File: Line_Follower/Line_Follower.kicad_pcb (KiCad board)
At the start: 2 copper layers, 109 x 110.5 mm, 20 parts, among them J1 Battery terminal, J10 Motor_B, J11 8-Channel IR Array, J9 Motor_A, SW1 Slide Switch, SW3 Mode, SW6 Calibration, U1 ESP32-DEVKITC, U2 LM2596 Buck Converter, U3 TB6612FNG_MD

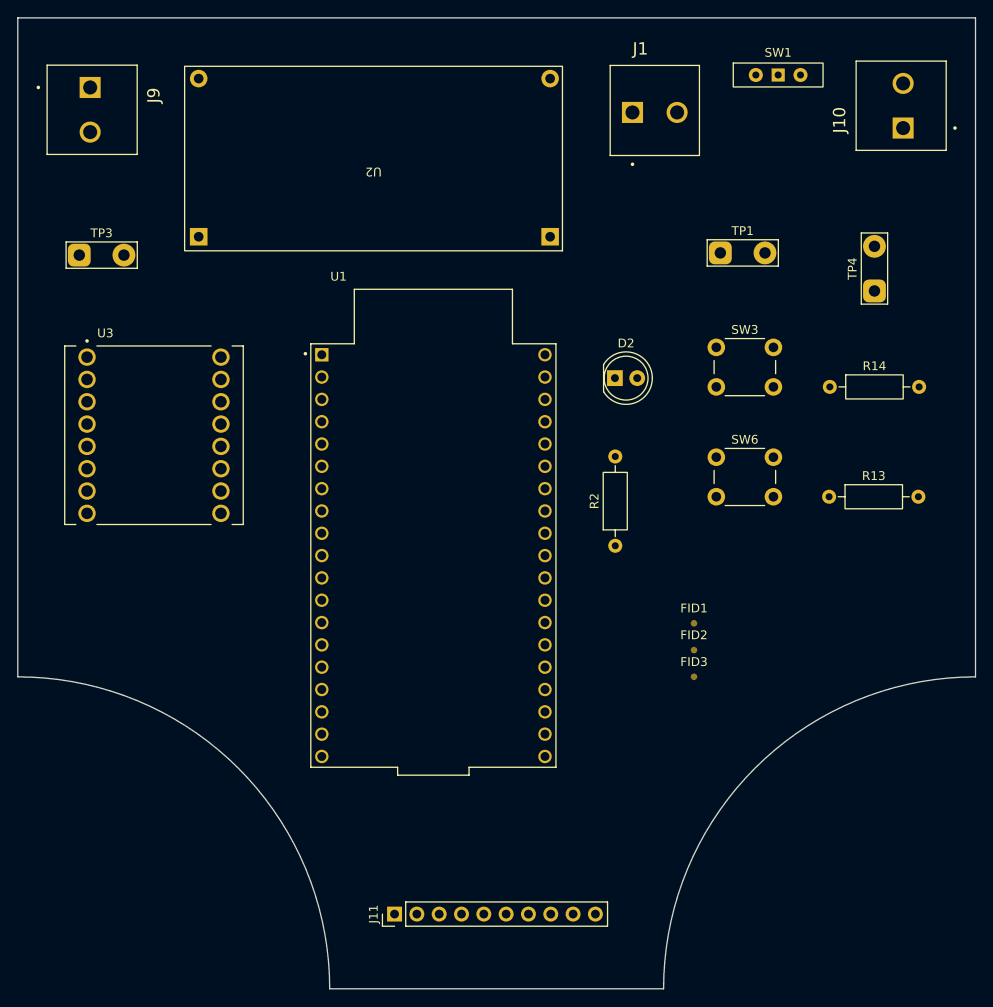
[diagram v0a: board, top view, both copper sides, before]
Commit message: PCB edge cuts designed
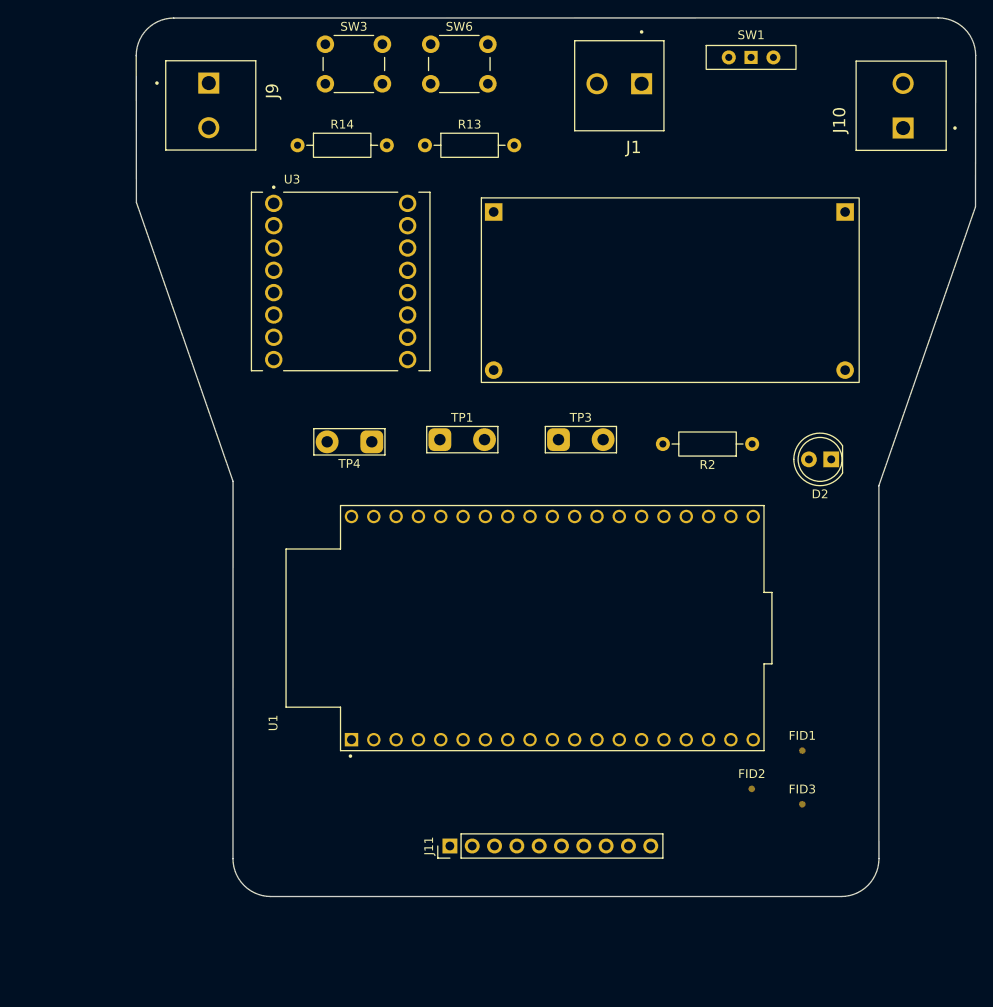
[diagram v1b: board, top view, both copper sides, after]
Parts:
- moved R14 66.5 mm to (116.8, 44.5)
- moved R13 61.0 mm to (131.3, 44.5)
- moved TP4 59.7 mm to (125.3, 78.2), turned to 180 degrees
- moved TP3 58.4 mm to (146.5, 78.0)
- moved SW6 57.1 mm to (132.0, 33.0)
- moved SW3 56.3 mm to (120.0, 33.0)
- moved TP1 38.3 mm to (133.0, 78.0)
- moved U2 37.1 mm to (137.8, 71.5), turned to 0 degrees
- moved U3 27.5 mm to (121.8, 60.0)
- moved D2 26.3 mm to (177.6, 80.2), turned to 180 degrees
- moved R2 19.4 mm to (168.6, 78.5), turned to 180 degrees
- moved FID1 19.0 mm to (174.3, 113.4)
- moved FID3 19.0 mm to (174.3, 119.5)
- moved FID2 17.1 mm to (168.5, 117.8)
- moved U1 15.9 mm to (145.8, 99.5), turned to 90 degrees
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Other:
- board size 109 x 110.5 mm -> 95.5 x 100 mm

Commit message: PCB updated
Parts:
- TP1: footprint TestPoint:TestPoint_2Pads_Pitch5.08mm_Drill1.3mm -> TestPoint:TestPoint_Pad_2.0x2.0mm
- TP2: renamed from TP4; footprint TestPoint:TestPoint_2Pads_Pitch5.08mm_Drill1.3mm -> TestPoint:TestPoint_Pad_2.0x2.0mm
- moved SW6 9.78 mm to (141.8, 33.8)
- moved R14 9.30 mm to (126.1, 45.5)
- moved SW3 9.30 mm to (129.2, 34.0)
- moved R13 9.06 mm to (140.3, 45.5)
- moved J1 4.75 mm to (160.8, 37.5)
- moved SW1 3.37 mm to (171.8, 34.0)
- moved U1 1.98 mm to (147.8, 99.7)
- moved U3 1.50 mm to (121.8, 61.5)
- moved U2 1.12 mm to (137.3, 72.5)
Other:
- board text added: "+"
- board text added: "+LED-"
- board text added: "-"
- board text added: "10K"
- board text added: "220"
- board text added: "3.3V"
- board text added: "Calib"
- board text added: "GND"
- board text added: "IR Array"
- board text added: "IR1"
- board text added: "IR2"
- board text added: "IR3"
- board text added: "IR4"
- board text added: "IR5"
- board text added: "IR6"
- board text added: "IR7"
- board text added: "IR8"
- board text added: "MA"
- board text added: "MB"
- board text added: "Mode"
- board text added: "Power"
- board text added: "V_BAT"

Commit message: PCB edited
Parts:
- removed FID1, FID2, FID3: Fiducial, Fiducial:Fiducial_0.75mm_Mask1.5mm
- removed TP3: TP_3V3, TestPoint:TestPoint_2Pads_Pitch5.08mm_Drill1.3mm
- moved TP1 44.8 mm to (119.8, 35.2), turned to 180 degrees
- moved TP2 43.3 mm to (125.2, 35.0), turned to 0 degrees
- moved D2 25.1 mm to (152.5, 78.8)
- moved SW3 2.71 mm to (132.0, 34.0)
- moved U2 1.75 mm to (135.5, 72.5)
- moved U1 1.74 mm to (146.6, 98.5)
- moved SW6 1.52 mm to (143.2, 34.0)
- moved U3 0.38 mm to (121.4, 61.5)
- moved SW1 0.37 mm to (172.1, 34.2)
- moved J1 0.37 mm to (161.0, 37.7)
- moved R13 0.37 mm to (140.6, 45.7)
- moved R14 0.37 mm to (126.4, 45.7)

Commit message: PCB updated
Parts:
- added H1: MountingHole, MountingHole:MountingHole_3.2mm_M3, F.Cu at (105.0, 54.5)
- added H2: MountingHole, MountingHole:MountingHole_3.2mm_M3, F.Cu at (187.5, 54.5)
- added H3: MountingHole, MountingHole:MountingHole_3.2mm_M3, F.Cu at (116.2, 115.8)
- added H4: MountingHole, MountingHole:MountingHole_3.2mm_M3, F.Cu at (176.2, 115.8)
- moved D2 41.7 mm to (176.2, 44.5)
- moved R2 29.2 mm to (167.8, 49.3), turned to 90 degrees
- moved J11 9.52 mm to (134.8, 114.8)
- moved U1 5.31 mm to (148.4, 93.5)
- moved U2 2.85 mm to (137.3, 74.7)
- moved U3 2.41 mm to (122.6, 63.6)
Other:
- board size 95.5 x 100 mm -> 95.5 x 93.5 mm
- board text removed: "IR Array"

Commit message: 3D models added
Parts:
- moved SW3 2.72 mm to (129.2, 34.3)
- moved SW6 2.72 mm to (140.5, 34.2)
- moved TP1 2.72 mm to (117.0, 35.5)
- moved TP2 2.72 mm to (122.5, 35.3)
- moved J1 2.72 mm to (158.3, 38.0)
- moved SW1 0.87 mm to (171.2, 34.2)
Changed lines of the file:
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@@
 	(footprint "Button_Switch_THT:SW_Slide-03_Wuerth-WS-SLTV_10x2.5x6.4_P2.54mm"
 		(layer "F.Cu")
-		(at 172.08 34.2375)
+		(at 171.21 34.2375)
 		(descr "Wuerth, WS-SLTV, 450301014042, https://www.we-online.com/components/products/datasheet/450301014042.pdf")
 		(tags "switch single-pole opposite-side-connection double-throw SPDT würth wurth")
@@
 			)
 		)
+		(model "D:/GitHUB/Line Follower/Hardware/External-3D-Models/Slide Switch/Mini Slide Switch.step"
+			(offset
+				(xyz 0 3 2.6)
+			)
+			(scale
+				(xyz 1 1 1)
+			)
+			(rotate
+				(xyz -180 -0 -0)
+			)
+		)
 	)
 	(footprint "Screw Terminal:CUI_TB007-508-02BE"
@@
 		(at 106.7375 37.42 -90)
 		(property "Reference" "J9"
-			(at 9.58 -0.2625 180)
+			(at 9.58 -0.2625 0)
 			(layer "F.SilkS")
 			(effects
@@
 		)
 		(property "Value" "Motor_A"
-			(at 9.58 -0.2625 180)
+			(at 9.58 -0.2625 0)
 			(layer "F.Fab")
 			(effects
@@
 		)
 		(embedded_fonts no)
+		(model "D:/GitHUB/Line Follower/Hardware/External-3D-Models/SCREW_TERMINAL_3DModel.STEP"
+			(offset
+				(xyz 5 5 0)
+			)
+			(scale
+				(xyz 1 1 1)
+			)
+			(rotate
+				(xyz -90 -0 90)
+			)
+		)
 	)
 	(footprint "Buck_Converter:LM2596_Buck_Module"
@@
 		)
 		(embedded_fonts no)
+		(model "D:/GitHUB/Line Follower/Hardware/External-3D-Models/LM2596/LM2596.STEP"
+			(offset
+				(xyz 21.515 10.5 0)
+			)
+			(scale
+				(xyz 1 1 1)
+			)
+			(rotate
+				(xyz -90 -0 -0)
+			)
+		)
 	)
 	(footprint "MountingHole:MountingHole_3.2mm_M3"
@@
 		(tags "mountinghole M3")
 		(property "Reference" "H2"
-			(at 0 -4.5 0)
+			(at -1.75 6.75 0)
 			(layer "F.SilkS")
 			(effects
@@
 		(tags "mountinghole M3")
 		(property "Reference" "H1"
-			(at 0 -4.5 0)
+			(at 1 6.5 0)
 			(layer "F.SilkS")
 			(effects
@@
 	(footprint "TestPoint:TestPoint_Pad_2.0x2.0mm"
 		(layer "F.Cu")
-		(at 125.25 35)
+		(at 122.54 35.2625)
 		(descr "SMD rectangular pad as test Point, square 2.0mm side length")
 		(tags "test point SMD pad rectangle square")
@@
 	(footprint "TestPoint:TestPoint_Pad_2.0x2.0mm"
 		(layer "F.Cu")
-		(at 119.75 35.25 180)
+		(at 117.04 35.5125 180)
 		(descr "SMD rectangular pad as test Point, square 2.0mm side length")
 		(tags "test point SMD pad rectangle square")
@@
 	(footprint "Button_Switch_THT:SW_PUSH_6mm"
 		(layer "F.Cu")
-		(at 131.96 34)
+		(at 129.25 34.2625)
 		(descr "Generic 6mm SW tactile push button")
 		(tags "tact sw push 6mm")
@@
 		)
 		(embedded_fonts no)
+		(model "D:/GitHUB/Line Follower/Hardware/External-3D-Models/TB6612FNG/Sparkfun Motor Driver.step"
+			(offset
+				(xyz 10.4 0 0)
+			)
+			(scale
+				(xyz 1 1 1)
+			)
+			(rotate
+				(xyz -0 -0 -0)
+			)
+		)
 	)
 	(footprint "Resistor_THT:R_Axial_DIN0207_L6.3mm_D2.5mm_P10.16mm_Horizontal"
@@
 	(footprint "Screw Terminal:CUI_TB007-508-02BE"
 		(layer "F.Cu")
-		(at 161.04 37.7375 180)
+		(at 158.33 38 180)
 		(property "Reference" "J1"
 			(at 0.905 -7.239 0)
@@
 		)
 		(embedded_fonts no)
+		(model "D:/GitHUB/Line Follower/Hardware/External-3D-Models/SCREW_TERMINAL_3DModel.STEP"
+			(offset
+				(xyz 5 5 0)
+			)
+			(scale
+				(xyz 1 1 1)
+			)
+			(rotate
+				(xyz -90 -0 90)
+			)
+		)
 	)
 	(footprint "Button_Switch_THT:SW_PUSH_6mm"
 		(layer "F.Cu")
-		(at 143.25 33.9875)
+		(at 140.54 34.25)
 		(descr "Generic 6mm SW tactile push button")
 		(tags "tact sw push 6mm")
@@
 	)
 	(gr_text "Calib"
-		(at 147.29 30.7375 180)
+		(at 144.58 31 180)
 		(layer "F.SilkS")
 		(effects
@@
 	)
 	(gr_text "+"
-		(at 161.04 31.9875 0)
+		(at 158.33 32.25 0)
 		(layer "F.SilkS")
 		(effects
@@
 	)
 	(gr_text "Power"
-		(at 174.54 30.9875 180)
+		(at 173.67 30.9875 180)
 		(layer "F.SilkS")
 		(effects
@@
 	)
 	(gr_text "GND"
-		(at 126.79 31.5 180)
+		(at 124.08 31.7625 180)
 		(layer "F.SilkS")
 		(effects
@@
 	)
 	(gr_text "-"
-		(at 155.29 31.9875 0)
+		(at 152.58 32.25 0)
 		(layer "F.SilkS")
 		(effects
@@
 	)
 	(gr_text "Mode"
-		(at 136 30.75 180)
+		(at 133.29 31.0125 180)
 		(layer "F.SilkS")
 		(effects
@@
 	)
 	(gr_text "V_BAT"
-		(at 121.75 31.5 180)
+		(at 119.04 31.7625 180)
 		(layer "F.SilkS")
 		(effects
